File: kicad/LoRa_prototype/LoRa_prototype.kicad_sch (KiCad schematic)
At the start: 5 parts, among them J2 U.FL, U3 AS179-92LF

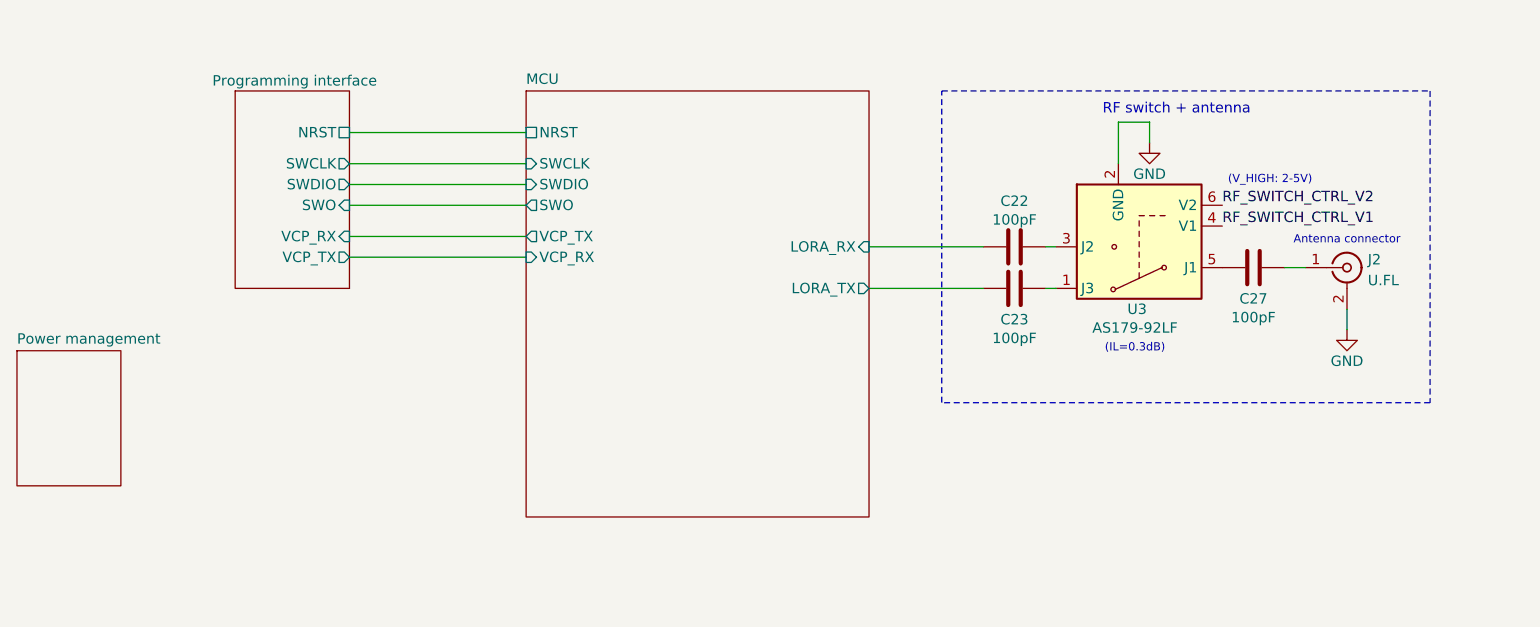
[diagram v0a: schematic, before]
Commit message: Done power block in schematics + ERC passed with 0 errors
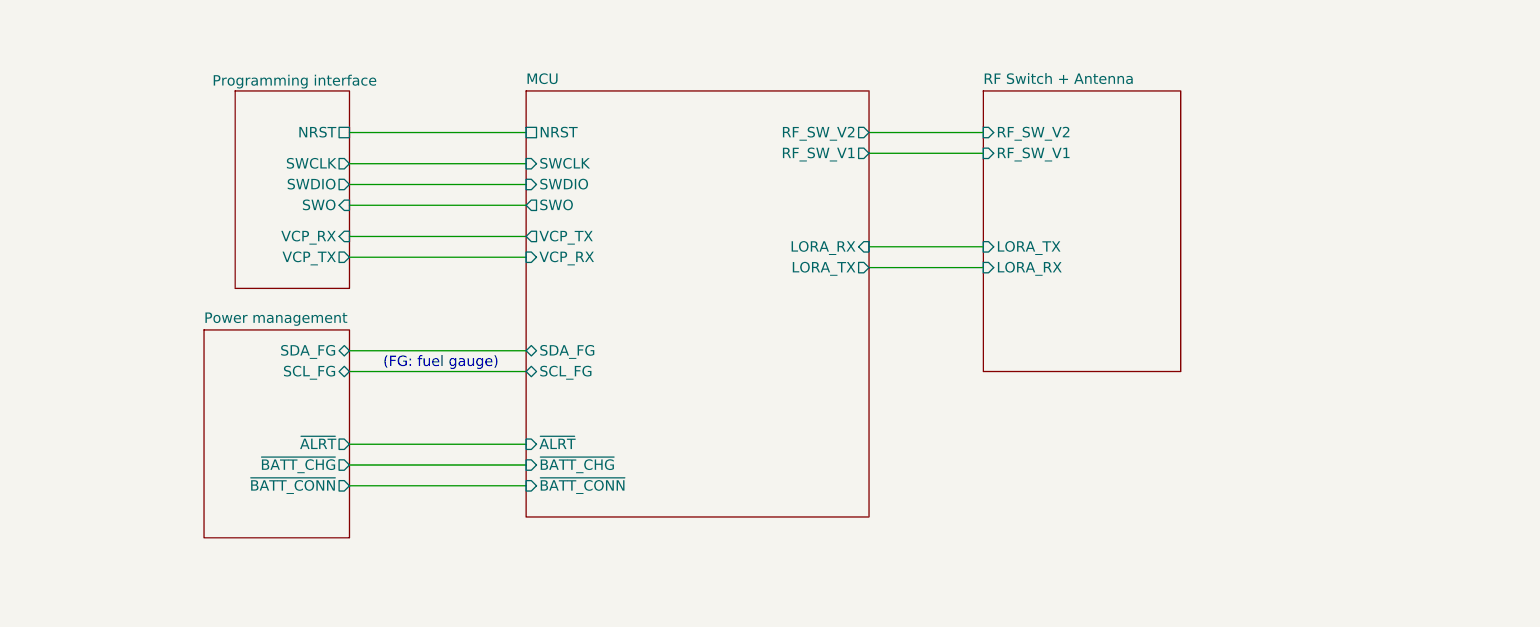
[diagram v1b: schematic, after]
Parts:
- removed C22, C23, C27: 100pF, symbol Device:C
- removed J2: U.FL, PCM_JLCPCB:IPEX-SMD_BWIPX-1-001E, symbol PCM_JLCPCB-Extended:RF, Connector, U.FL
- removed U3: AS179-92LF, Package_TO_SOT_SMD:SOT-363_SC-70-6, symbol RF_Switch:AS179-92LF
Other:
- added sheet RF Switch + Antenna (antenna.kicad_sch)
- sheet MCU ports: added RF_SW_V1, RF_SW_V2, SCL_FG, SDA_FG, ~{ALRT}, ~{BATT_CHG}, ~{BATT_CONN}; removed none
- sheet Power management ports: added SCL_FG, SDA_FG, ~{ALRT}, ~{BATT_CHG}, ~{BATT_CONN}; removed none
- note added: "(FG: fuel gauge)"
- note removed: "(IL=0.3dB)"
- note removed: "(V_HIGH: 2-5V)"
- note removed: "Antenna connector"
- note removed: "RF switch + antenna"

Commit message: Start schematic for GPS module
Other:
- added sheet GPS (gps.kicad_sch)
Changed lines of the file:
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@@
+	)
+	(sheet
+		(at 195.58 109.22)
+		(size 17.78 22.86)
+		(exclude_from_sim no)
+		(in_bom yes)
+		(on_board yes)
+		(dnp no)
+		(fields_autoplaced yes)
+		(stroke
+			(width 0.1524)
+			(type solid)
+		)
+		(fill
+			(color 212 212 212 1.0000)
+		)
+		(property "Sheetname" "GPS"
+			(at 195.58 108.5084 0)
+			(effects
+				(font
+					(size 1.27 1.27)
+				)
+				(justify left bottom)
+			)
+		)
+		(property "Sheetfile" "gps.kicad_sch"
+			(at 195.58 132.6646 0)
+			(effects
+				(font
+					(size 1.27 1.27)
+				)
+				(justify left top)
+			)
+		)
+		(instances
+			(project "LoRa_prototype"
+				(path "/9fad4700-f514-47ad-821a-b4076ecc08de"
+					(page "6")
+				)
+			)
+		)
 	)
 	(sheet

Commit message: Done schematic GPS block with 0 ERC errors (Milestone)
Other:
- sheet GPS ports: added GPS_RX, GPS_TX, GPS_~{RESET}; removed none
- sheet MCU ports: added GPS_~{RESET}, RX1, TX1; removed none
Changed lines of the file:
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@@
+	(wire
+		(pts
+			(xy 138.43 116.84) (xy 152.4 116.84)
+		)
+		(stroke
+			(width 0)
+			(type default)
+		)
+	)
 	(wire
 		(pts
@@
 	(wire
 		(pts
+			(xy 138.43 119.38) (xy 152.4 119.38)
+		)
+		(stroke
+			(width 0)
+			(type default)
+		)
+	)
+	(wire
+		(pts
 			(xy 74.93 90.17) (xy 96.52 90.17)
 		)
@@
 		)
 	)
+	(wire
+		(pts
+			(xy 138.43 124.46) (xy 152.4 124.46)
+		)
+		(stroke
+			(width 0)
+			(type default)
+		)
+	)
 	(sheet
-		(at 195.58 109.22)
+		(at 152.4 114.3)
 		(size 17.78 22.86)
 		(exclude_from_sim no)
@@
 		)
 		(property "Sheetname" "GPS"
-			(at 195.58 108.5084 0)
+			(at 152.4 113.5884 0)
 			(effects
 				(font
@@
 		)
 		(property "Sheetfile" "gps.kicad_sch"
-			(at 195.58 132.6646 0)
+			(at 152.4 137.7446 0)
 			(effects
 				(font
@@
 				)
 				(justify left top)
+				(hide yes)
+			)
+		)
+		(pin "GPS_RX" bidirectional
+			(at 152.4 116.84 180)
+			(effects
+				(font
+					(size 1.27 1.27)
+				)
+				(justify left)
+			)
+		)
+		(pin "GPS_TX" bidirectional
+			(at 152.4 119.38 180)
+			(effects
+				(font
+					(size 1.27 1.27)
+				)
+				(justify left)
+			)
+		)
+		(pin "GPS_~{RESET}" input
+			(at 152.4 124.46 180)
+			(effects
+				(font
+					(size 1.27 1.27)
+				)
+				(justify left)
 			)
 		)
@@
 			(effects
 				(font
+					(size 1.27 1.27)
+				)
+				(justify right)
+			)
+		)
+		(pin "TX1" bidirectional
+			(at 138.43 116.84 0)
+			(effects
+				(font
+					(size 1.27 1.27)
+				)
+				(justify right)
+			)
+		)
+		(pin "RX1" bidirectional
+			(at 138.43 119.38 0)
+			(effects
+				(font
+					(size 1.27 1.27)
+				)
+				(justify right)
+			)
+		)
+		(pin "GPS_~{RESET}" output
+			(at 138.43 124.46 0)
+			(effects
+				(font

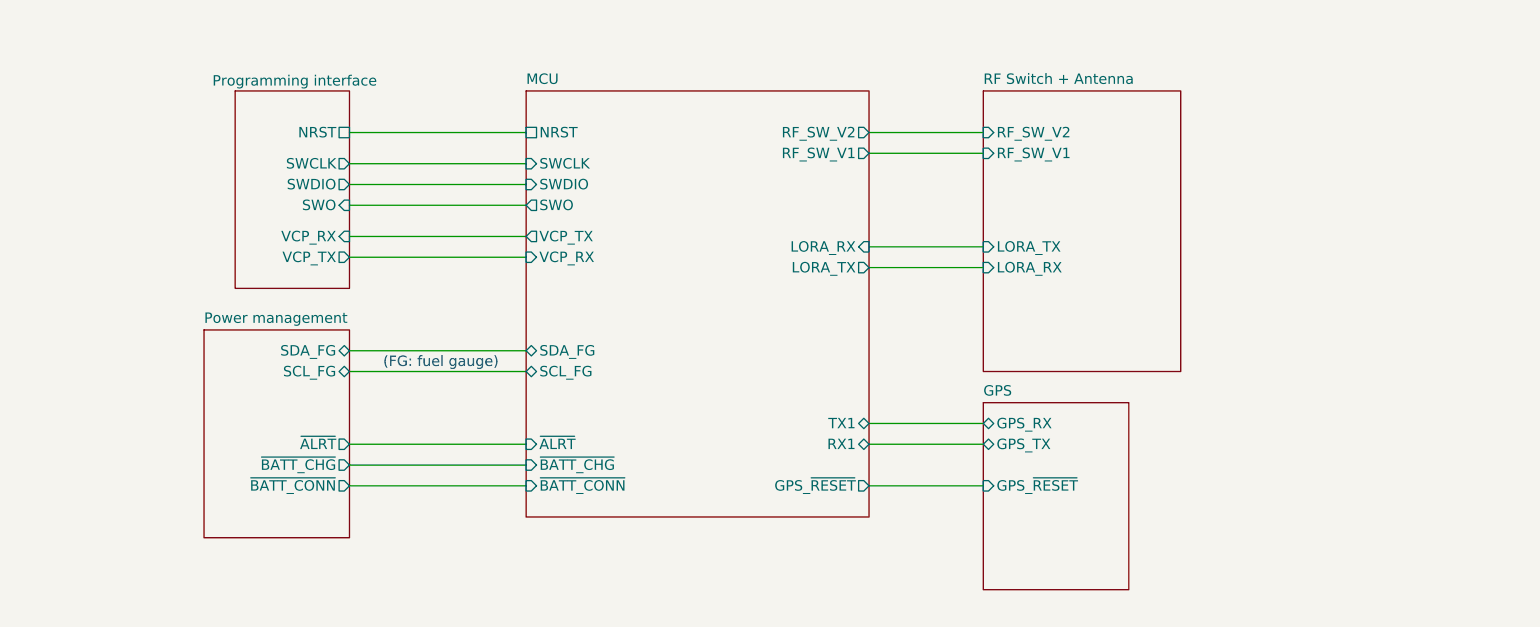
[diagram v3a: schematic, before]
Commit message: Copied and cleaned up USb charging circuit from WORK-CARE
1 ERC error
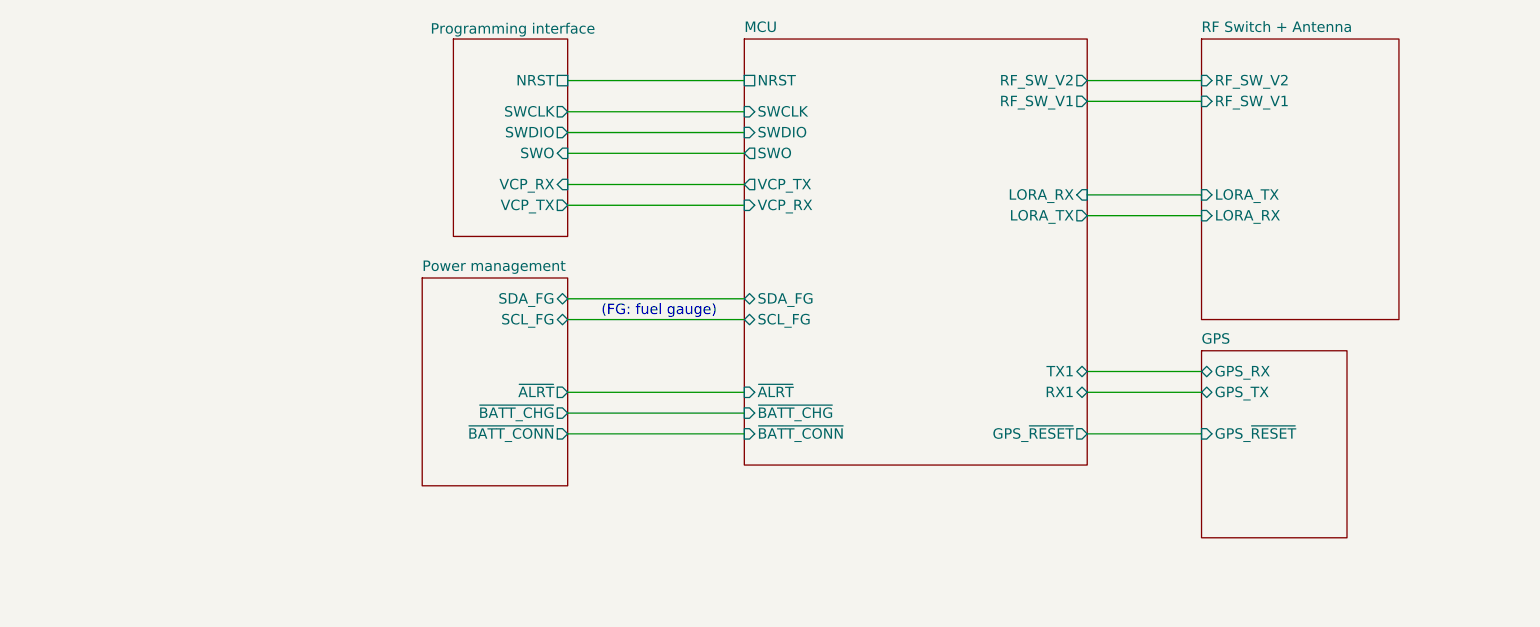
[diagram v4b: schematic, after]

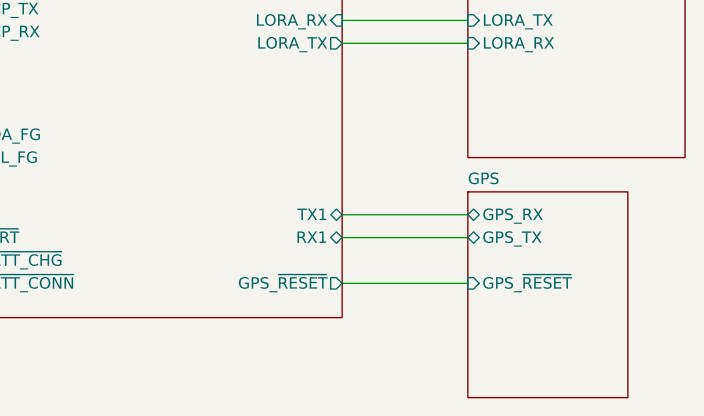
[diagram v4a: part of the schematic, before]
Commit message: Added I2C pullups for fuel guage
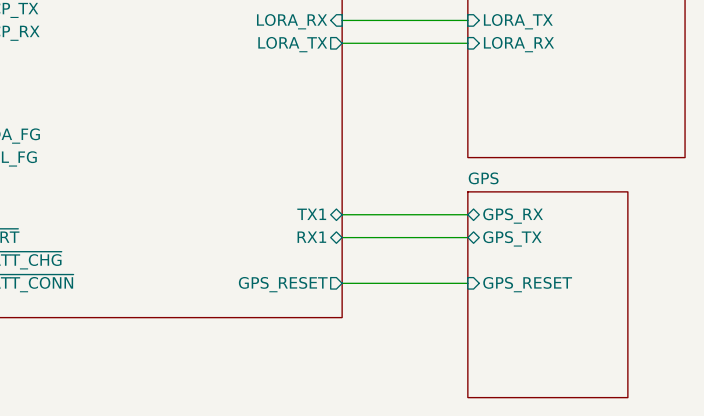
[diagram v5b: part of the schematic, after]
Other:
- sheet GPS ports: added GPS_RESET; removed GPS_~{RESET}
- sheet MCU ports: added GPS_RESET; removed GPS_~{RESET}
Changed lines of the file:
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@@
 			)
 		)
-		(pin "GPS_~{RESET}" input
+		(pin "GPS_RESET" input
 			(at 179.07 118.11 180)
 			(effects
@@
 			)
 		)
-		(pin "GPS_~{RESET}" output
+		(pin "GPS_RESET" output
 			(at 165.1 118.11 0)
 			(effects

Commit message: Done schematic for GPS and gas sensors (Milestone)
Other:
- sheet GPS ports: added SCK_BMV, SCL_BME, SDA_BME, SDA_BMV; removed none
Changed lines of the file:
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@@
 	(sheet
 		(at 179.07 107.95)
-		(size 17.78 22.86)
+		(size 24.13 27.94)
 		(exclude_from_sim no)
 		(in_bom yes)
@@
 		)
 		(property "Sheetfile" "gps.kicad_sch"
-			(at 179.07 131.3946 0)
+			(at 179.07 136.4746 0)
 			(effects
 				(font
@@
 			(effects
 				(font
+					(size 1.27 1.27)
+				)
+				(justify left)
+			)
+		)
+		(pin "SCK_BMV" input
+			(at 179.07 121.92 180)
+			(effects
+				(font
+					(size 1.27 1.27)
+				)
+				(justify left)
+			)
+		)
+		(pin "SDA_BMV" bidirectional
+			(at 179.07 124.46 180)
+			(effects
+				(font
+					(size 1.27 1.27)
+				)
+				(justify left)
+			)
+		)
+		(pin "SCL_BME" input
+			(at 179.07 127 180)
+			(effects
+				(font
+					(size 1.27 1.27)
+				)
+				(justify left)
+			)
+		)
+		(pin "SDA_BME" bidirectional
+			(at 179.07 129.54 180)
+			(effects
+				(font

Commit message: Schematic cleanup (0 ERC violations)
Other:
- sheet MCU ports: added SCL1, SDA1; removed SCL_FG, SDA_FG

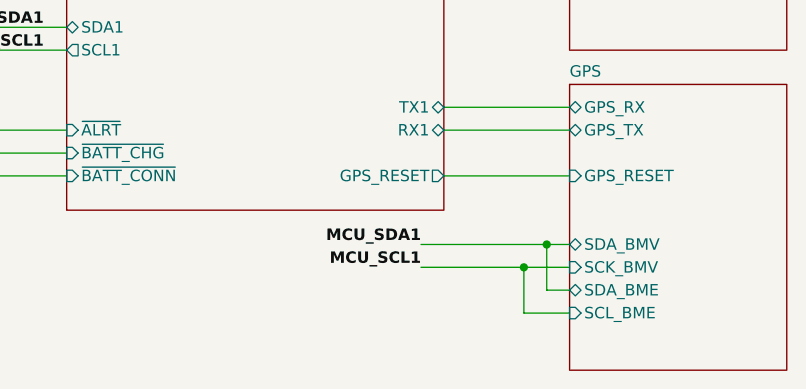
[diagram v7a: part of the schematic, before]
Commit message: Done schematic with 0 ERC errors (Milestone)
Still need to double/triple check tho
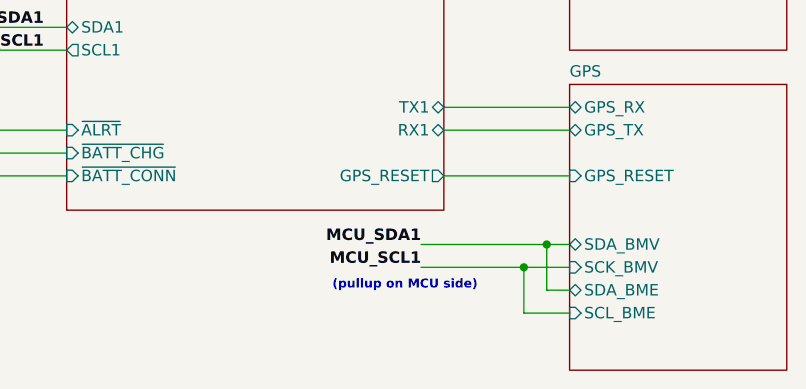
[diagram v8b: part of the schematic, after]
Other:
- note added: "(pullup on MCU side)"
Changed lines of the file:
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@@
+		)
+	)
+	(text "(pullup on MCU side)"
+		(exclude_from_sim no)
+		(at 160.782 130.302 0)
+		(effects
+			(font
+				(size 1 1)
+				(thickness 0.254)
+				(bold yes)
+			)
 		)
 	)
